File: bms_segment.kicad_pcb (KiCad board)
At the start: 4 copper layers, 100 x 67 mm, 167 parts, among them J1 Conn_01x13, J2 Conn_01x04, J3 Conn_02x10_Odd_Even, J4 Conn_02x10_Odd_Even, J5 Conn_01x05, J6 Conn_01x04, Q1 IRLML0060, Q10 IRLML0060, Q11 IRLML0060, Q12 IRLML0060, Q2 IRLML0060, Q3 IRLML0060, Q4 IRLML0060, Q5 IRLML0060, Q6 IRLML0060, Q7 IRLML0060, Q8 IRLML0060, Q9 IRLML0060, SW1 SW_Push, U1 LMR516xx, U2 STM32F103C8Tx, U3 ADuM1252, U4 MAX14920, U5 MAX11163, U6 REF61xx, U7 TCA9535PWR, Y1 8M

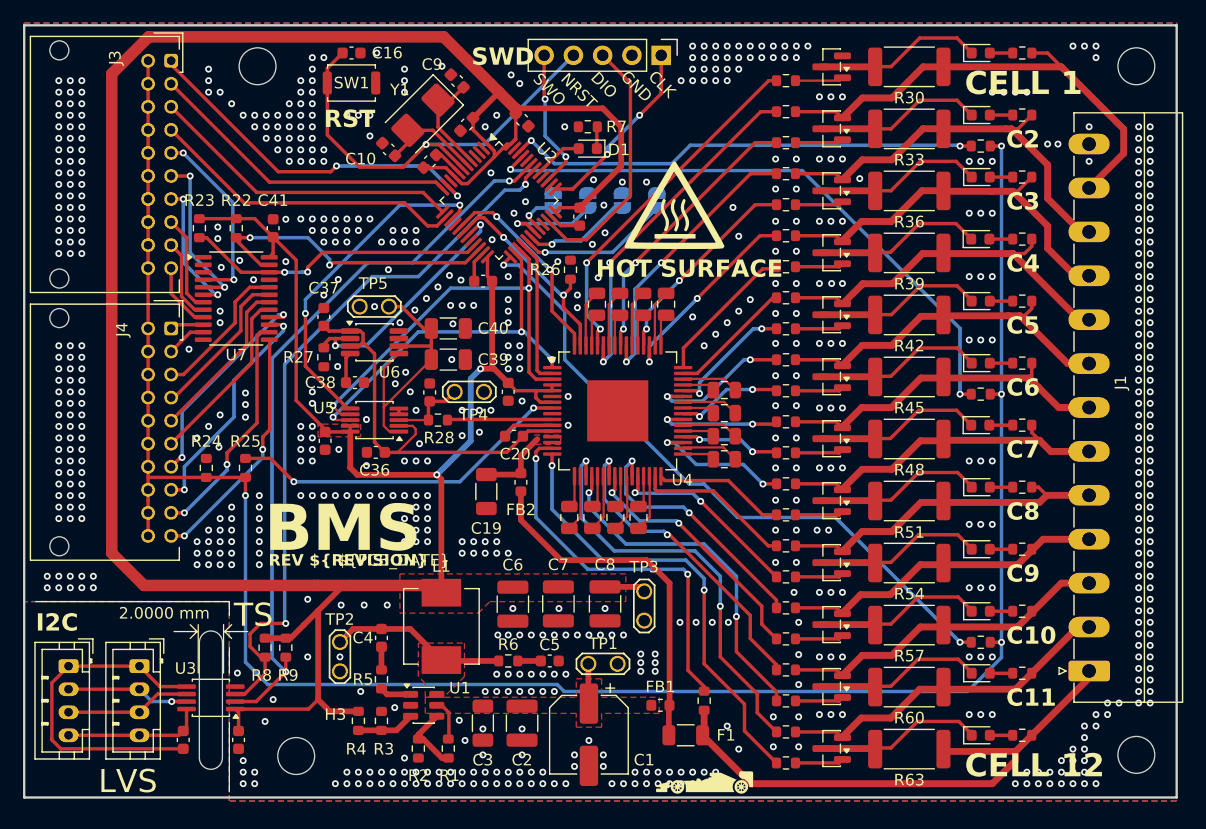
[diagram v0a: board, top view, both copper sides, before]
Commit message: *: Create a 3V3 plane and switch to new reset button
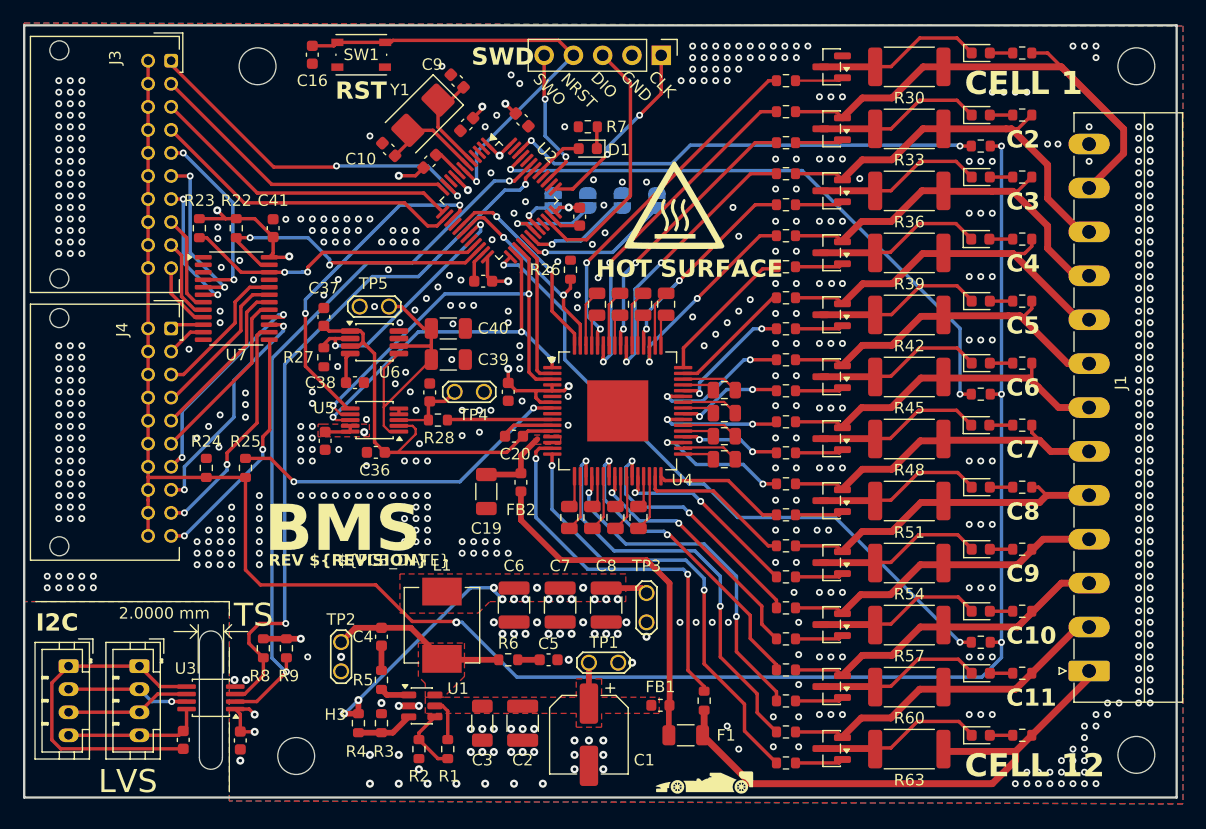
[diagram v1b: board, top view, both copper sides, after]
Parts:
- SW1: footprint Button_Switch_SMD:SW_Push_SPST_NO_Alps_SKRK -> Button_Switch_SMD:SW_Push_1P1T_NO_Vertical_Wuerth_434133025816
- moved C16 3.40 mm to (70.0, 56.8), turned to -90 degrees
- moved SW1 2.59 mm to (74.2, 56.8)
- moved TP3 0.25 mm to (99.0, 106.0)
- moved R3 0.20 mm to (76.0, 114.8)
- moved R4 0.20 mm to (74.0, 114.8)
- moved C7 0.18 mm to (91.5, 104.5)
- moved U1 0.17 mm to (79.5, 113.2)
- moved R8 0.16 mm to (65.8, 108.2)
- moved C17 0.16 mm to (63.8, 116.2)
- moved C8 0.14 mm to (95.5, 104.5)
- moved C5 0.14 mm to (90.5, 109.2)
- moved C6 0.12 mm to (87.5, 104.5)
- moved L1 0.11 mm to (81.2, 106.2)
- moved TP1 0.11 mm to (94.0, 109.5)
- moved TP2 0.10 mm to (72.5, 110.2)
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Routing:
- net +3V3: track 269.1 -> 73.7 mm, vias 2 -> 29
- net T2: track 181.0 -> 175.3 mm
- net /NRST: track 38.3 -> 39.0 mm
- net GND: vias 730 -> 607
- added copper zone on In2.Cu, net +3V3

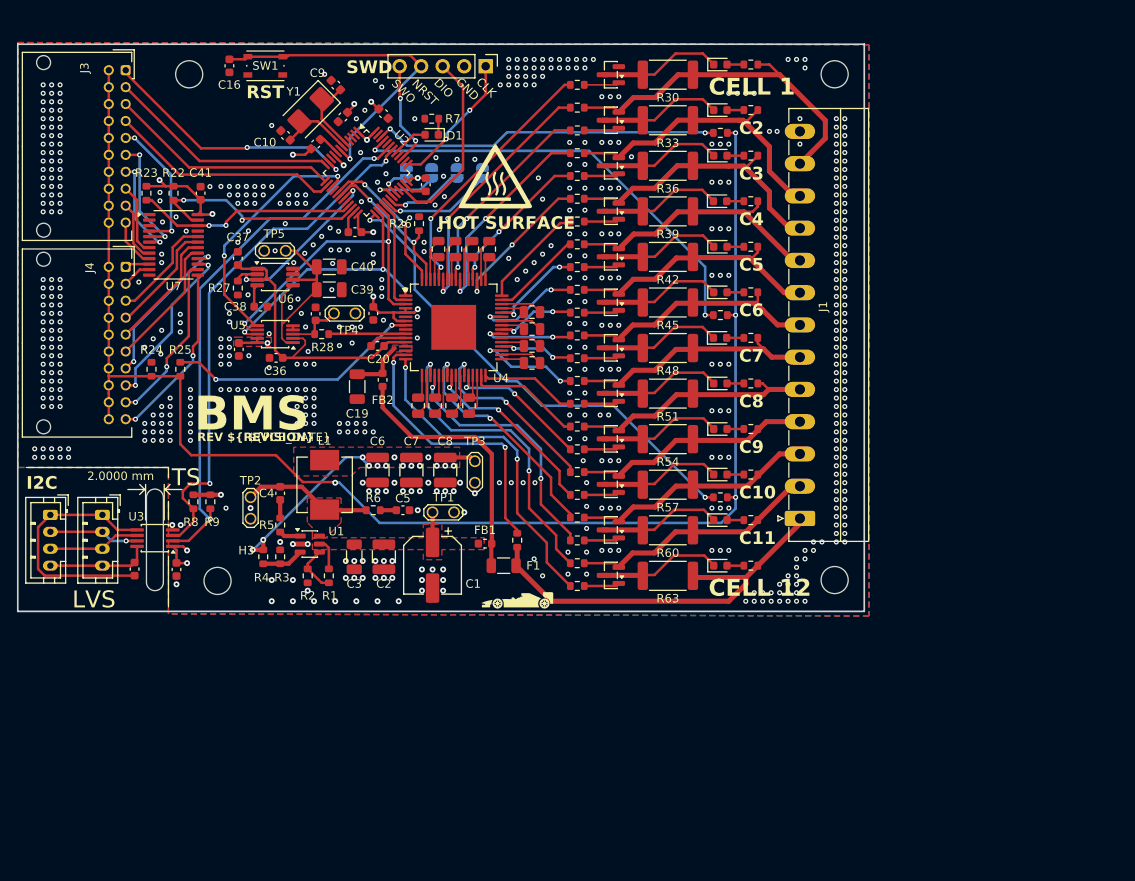
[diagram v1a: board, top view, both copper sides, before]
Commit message: pcb: Create blank PCB
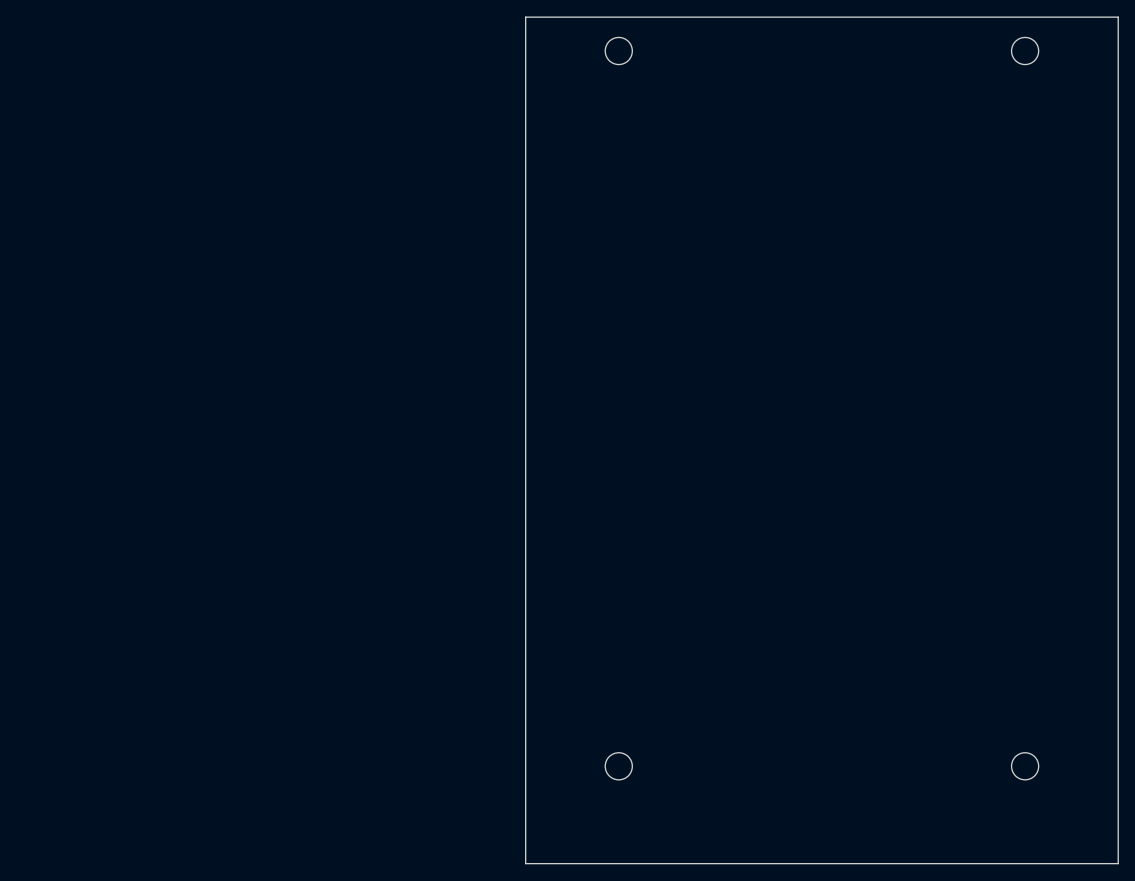
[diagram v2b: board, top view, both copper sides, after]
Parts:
- removed C1: 22u, Capacitor_SMD:CP_Elec_6.3x7.7
- removed C10, C9: 30p, Capacitor_SMD:C_0603_1608Metric
- removed C11, C12, C13, C14, C15, C20, C21, C38, C41: 1u, Capacitor_SMD:C_0603_1608Metric
- removed C16, C17, C18, C35, C36, C37, C4: 100n, Capacitor_SMD:C_0603_1608Metric
- removed C19, C3: 100n, Capacitor_SMD:C_1206_3216Metric
- removed C2: 2u2, Capacitor_SMD:C_1210_3225Metric
- removed C22, C23, C24, C25, C26, C27, C28, C29, C30, C31, C32, C33: 1u, Capacitor_SMD:C_0805_2012Metric
- removed C34: 100p, Capacitor_SMD:C_0603_1608Metric
- removed C39, C40: 10u, Capacitor_SMD:C_1206_3216Metric
- removed C5: ?, Capacitor_SMD:C_0603_1608Metric
- removed C6, C7, C8: 22u, Capacitor_SMD:C_1210_3225Metric
- removed D1, D10, D11, D12, D13, D2, D3, D4, D5, D6, D7, D8, D9: LED_Small, LED_SMD:LED_0603_1608Metric
- removed F1: Polyfuse, Resistor_SMD:R_1206_3216Metric
- removed FB1: 600, Inductor_SMD:L_0603_1608Metric
- removed FB2: 220, Inductor_SMD:L_0603_1608Metric
- removed G***, G****: LOGO, LOGO
- removed J1: Conn_01x13, Connector_Phoenix_MC:PhoenixContact_MC_1,5_13-G-3.81_1x13_P3.81mm_Horizontal
- removed J2, J6: Conn_01x04, Connector_JST:JST_PH_B4B-PH-K_1x04_P2.00mm_Vertical
- removed J3, J4: Conn_02x10_Odd_Even, Connector_JST:JST_PUD_S20B-PUDSS-1_2x10_P2.00mm_Horizontal
- removed J5: Conn_01x05, Connector_PinHeader_2.54mm:PinHeader_1x05_P2.54mm_Vertical
- removed JP1, JP2, JP3, JP4: SolderJumper_2_Open, Jumper:SolderJumper-2_P1.3mm_Open_RoundedPad1.0x1.5mm
- removed L1: 22u, Inductor_SMD:L_Vishay_IHLP-2525
- removed Q1, Q10, Q11, Q12, Q2, Q3, Q4, Q5, Q6, Q7, Q8, Q9: IRLML0060, Package_TO_SOT_SMD:SOT-23
- removed R1: 10M, Resistor_SMD:R_0603_1608Metric
- removed R10, R11, R12, R13, R14, R15, R16, R17, R18, R19, R20, R21, R29, R32, R35, R38, R41, R44, R47, R50, R53, R56, R59, R62: 3k, Resistor_SMD:R_0603_1608Metric
- removed R2: 390k, Resistor_SMD:R_0603_1608Metric
- removed R22, R23, R26, R27, R8, R9: 100k, Resistor_SMD:R_0603_1608Metric
- removed R24, TH1, TH2, TH3: 10k, Resistor_SMD:R_0603_1608Metric
- removed R25: 1k, Resistor_SMD:R_0603_1608Metric
- removed R28: 220, Resistor_SMD:R_0603_1608Metric
- removed R3: 24k, Resistor_SMD:R_0603_1608Metric
- removed R30, R33, R36, R39, R42, R45, R48, R51, R54, R57, R60, R63: 20, Resistor_SMD:R_2512_6332Metric
- removed R31, R34, R37, R40, R43, R46, R49, R52, R55, R58, R61, R64, R7: 330, Resistor_SMD:R_0603_1608Metric
- removed R4: 75k, Resistor_SMD:R_0603_1608Metric
- removed R5: 6R8, Resistor_SMD:R_0603_1608Metric
- removed R6: ?, Resistor_SMD:R_0603_1608Metric
- removed SW1: SW_Push, Button_Switch_SMD:SW_Push_1P1T_NO_Vertical_Wuerth_434133025816
- removed TP1, TP2, TP3, TP4, TP5: TestPoint_2Pole, yfs:TestPoint_2Pads_Pitch2.54mm_Drill1.0mm
- removed U1: LMR516xx, Package_TO_SOT_SMD:SOT-23-6
- removed U2: STM32F103C8Tx, Package_QFP:LQFP-48_7x7mm_P0.5mm
- removed U3: ADuM1252, Package_SO:MSOP-8_3x3mm_P0.65mm
- removed U4: MAX14920, Package_QFP:TQFP-64-1EP_10x10mm_P0.5mm_EP5.305x5.305mm
- removed U5: MAX11163, Package_SO:MSOP-10_3x3mm_P0.5mm
- removed U6: REF61xx, Package_SO:VSSOP-8_3x3mm_P0.65mm
- removed U7: TCA9535PWR, Package_SO:TSSOP-24_4.4x7.8mm_P0.65mm
- removed Y1: 8M, Crystal:Crystal_SMD_5032-2Pin_5.0x3.2mm
- moved H4 128.2 mm to (164.0, 139.5)
- moved H1 67.5 mm to (116.0, 55.0)
- moved H3 52.2 mm to (116.0, 139.5)
- moved H2 22.7 mm to (164.0, 55.0)
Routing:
- net T2: track 175.3 -> 0.00 mm, vias 4 -> 0
- net +3V3: track 73.7 -> 0.00 mm, vias 29 -> 0
- net /SDA: track 63.9 -> 0.00 mm, vias 2 -> 0
- net /SCL: track 62.4 -> 0.00 mm, vias 2 -> 0
- net /Thermistors/TH2: track 57.6 -> 0.00 mm, vias 2 -> 0
- net /Thermistors/TH1: track 53.0 -> 0.00 mm, vias 2 -> 0
- net TAP12: track 48.7 -> 0.00 mm
- net TAP1: track 42.2 -> 0.00 mm
- net /Thermistors/TH0: track 41.2 -> 0.00 mm, vias 2 -> 0
- net BA12: track 39.1 -> 0.00 mm, vias 2 -> 0
- net /NRST: track 39.0 -> 0.00 mm, vias 1 -> 0
- net Net-(U4-CV11): track 36.3 -> 0.00 mm, vias 2 -> 0
- net MISO: track 36.2 -> 0.00 mm, vias 2 -> 0
- net TAP3: track 35.9 -> 0.00 mm
- net TAP2: track 35.7 -> 0.00 mm
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- removed copper zone on F.Cu, net +3V3
- removed copper zone on In2.Cu, net +3V3
- removed copper zone on F.Cu, net /AFE_VIN
- removed copper zone on F.Cu, net /BUCK_SW
- removed copper zone on F.Cu, net /BUCK_VIN
- removed copper zone on B.Cu, net GND
- removed copper zone on F.Cu, net GND
- removed copper zone on In1.Cu, net GND
- removed copper zone on In2.Cu, net GND
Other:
- board size 100 x 67 mm -> 70 x 100 mm
- board text removed: "${PCB_DATE}"
- board text removed: "2.0000 mm"
- board text removed: "A0"
- board text removed: "A1"
- board text removed: "A2"
- board text removed: "A3"
- board text removed: "BMS"
- board text removed: "BY LOGAN C + OWEN S"
- board text removed: "C10"
- board text removed: "C11"
- board text removed: "C2"
- board text removed: "C3"
- board text removed: "C4"
- board text removed: "C5"
- board text removed: "C6"
- board text removed: "C7"
- board text removed: "C8"
- board text removed: "C9"
- board text removed: "CELL 1"
- board text removed: "CELL 12"
- board text removed: "CLK"
- board text removed: "DIO"
- board text removed: "DISTRIBUTED BMS"
- board text removed: "GND"
- board text removed: "HOT SURFACE"
- board text removed: "I2C"
- board text removed: "LVS"
- board text removed: "NRST"
- board text removed: "REV ${REVISION}"
- board text removed: "RST"
- board text removed: "SWD"
- board text removed: "SWO"
- board text removed: "TS"
- board text removed: "{ "ViaStitching": "0.2", "stitch_zone_0": { "HSpacing": "1", "VSpacing": "1", "HOffset": "0", "VOffset": "", "Clearance": "1", "Randomize": true } }"
- board text removed: "{ "ViaStitching": "0.2", "stitch_zone_0": { "HSpacing": "1", "VSpacing": "1", "HOffset": "0", "VOffset": "0", "Clearance": "0.75", "Randomize": false } }"
- board text removed: "{ "ViaStitching": "0.2", "stitch_zone_0": { "HSpacing": "1", "VSpacing": "1", "HOffset": "0", "VOffset": "0", "Clearance": "1", "Randomize": false } }"
- board text removed: "{ "ViaStitching": "0.2", "stitch_zone_0": { "HSpacing": "2", "VSpacing": "2", "HOffset": "1", "VOffset": "1", "Clearance": "0", "Randomize": false } }"

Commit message: pcb: Add progress so far
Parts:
- added C1: 22u, Capacitor_SMD:CP_Elec_6.3x7.7, F.Cu at (135.2, 52.5)
- added C10: 1u, Capacitor_SMD:C_0603_1608Metric, F.Cu at (41.3, 101.0)
- added C11: 100n, Capacitor_SMD:C_1206_3216Metric, F.Cu at (86.5, 111.0)
- added C12: 1u, Capacitor_SMD:C_0805_2012Metric, F.Cu at (61.5, 98.8)
- added C13: 1u, Capacitor_SMD:C_0805_2012Metric, F.Cu at (61.5, 101.8)
- added C14: 1u, Capacitor_SMD:C_0805_2012Metric, F.Cu at (61.5, 104.8)
- added C15: 1u, Capacitor_SMD:C_0805_2012Metric, F.Cu at (61.5, 107.8)
- added C16: 1u, Capacitor_SMD:C_0805_2012Metric, F.Cu at (66.0, 98.8)
- added C17: 1u, Capacitor_SMD:C_0805_2012Metric, F.Cu at (66.0, 101.8)
- added C18: 1u, Capacitor_SMD:C_0805_2012Metric, F.Cu at (66.0, 104.8)
- added C19: 1u, Capacitor_SMD:C_0805_2012Metric, F.Cu at (66.0, 107.8)
- added C2: 2u2, Capacitor_SMD:C_1210_3225Metric, F.Cu at (141.0, 53.5)
- added C20: 1u, Capacitor_SMD:C_0805_2012Metric, F.Cu at (70.4, 98.8)
- added C21: 1u, Capacitor_SMD:C_0805_2012Metric, F.Cu at (70.4, 101.8)
- added C22: 1u, Capacitor_SMD:C_0805_2012Metric, F.Cu at (70.4, 104.8)
- added C23: 1u, Capacitor_SMD:C_0805_2012Metric, F.Cu at (70.4, 107.8)
- added C24: 1u, Capacitor_SMD:C_0805_2012Metric, F.Cu at (74.9, 98.8)
- added C25: 1u, Capacitor_SMD:C_0805_2012Metric, F.Cu at (74.9, 101.8)
- added C26: 1u, Capacitor_SMD:C_0805_2012Metric, F.Cu at (74.9, 104.8)
- added C27: 1u, Capacitor_SMD:C_0805_2012Metric, F.Cu at (74.9, 107.8)
- added C28: 100p, Capacitor_SMD:C_0603_1608Metric, F.Cu at (45.3, 103.5)
- added C29: 100n, Capacitor_SMD:C_0603_1608Metric, F.Cu at (45.3, 108.5)
- added C3: 100n, Capacitor_SMD:C_1206_3216Metric, F.Cu at (144.5, 53.5)
- added C30: 100n, Capacitor_SMD:C_0603_1608Metric, F.Cu at (45.3, 111.0)
- added C31: 100n, Capacitor_SMD:C_0603_1608Metric, F.Cu at (45.3, 113.6)
- added C32: 1u, Capacitor_SMD:C_0603_1608Metric, F.Cu at (45.3, 106.0)
- added C33: 10u, Capacitor_SMD:C_1206_3216Metric, F.Cu at (86.5, 114.3)
- added C34: 10u, Capacitor_SMD:C_1206_3216Metric, F.Cu at (86.5, 117.7)
- added C35: 1u, Capacitor_SMD:C_0603_1608Metric, F.Cu at (41.3, 106.0)
- added C36: 1u, Capacitor_SMD:C_0603_1608Metric, F.Cu at (41.3, 111.0)
- added C37: 1u, Capacitor_SMD:C_0603_1608Metric, F.Cu at (41.3, 113.6)
- added C38: 1u, Capacitor_SMD:C_0603_1608Metric, F.Cu at (41.3, 116.1)
- added C39: 1u, Capacitor_SMD:C_0603_1608Metric, F.Cu at (45.3, 98.5)
- added C4: 100n, Capacitor_SMD:C_0603_1608Metric, F.Cu at (153.2, 61.0)
- added C40: 100n, Capacitor_SMD:C_0603_1608Metric, F.Cu at (45.3, 101.0)
- added C41: 100n, Capacitor_SMD:C_0603_1608Metric, F.Cu at (41.3, 103.5)
- added C42: 100n, Capacitor_SMD:C_0603_1608Metric, F.Cu at (41.3, 108.5)
- added C43: ?, Capacitor_SMD:C_0603_1608Metric, F.Cu at (76.4, 127.3)
- added C44: ?, Capacitor_SMD:C_0603_1608Metric, F.Cu at (76.4, 129.8)
- added C45: ?, Capacitor_SMD:C_0603_1608Metric, F.Cu at (76.4, 132.4)
- added C46: ?, Capacitor_SMD:C_0603_1608Metric, F.Cu at (76.4, 134.9)
- added C47: 1u, Capacitor_SMD:C_0603_1608Metric, F.Cu at (93.2, 98.0)
- added C48: 1u, Capacitor_SMD:C_0603_1608Metric, F.Cu at (93.2, 100.5)
- added C49: 1u, Capacitor_SMD:C_0603_1608Metric, F.Cu at (93.2, 103.0)
- added C5: ?, Capacitor_SMD:C_0603_1608Metric, F.Cu at (138.8, 59.0)
- added C6: 22u, Capacitor_SMD:C_1210_3225Metric, F.Cu at (141.8, 63.8)
- added C7: 22u, Capacitor_SMD:C_1210_3225Metric, F.Cu at (137.8, 63.8)
- added C8: 22u, Capacitor_SMD:C_1210_3225Metric, F.Cu at (133.8, 63.8)
- added C9: 1u, Capacitor_SMD:C_0603_1608Metric, F.Cu at (41.3, 98.5)
- added D1: LED_Small, LED_SMD:LED_0603_1608Metric, F.Cu at (122.0, 132.0)
- added D10: LED_Small, LED_SMD:LED_0603_1608Metric, F.Cu at (122.0, 91.5)
- added D11: LED_Small, LED_SMD:LED_0603_1608Metric, F.Cu at (122.0, 87.0)
- added D12: LED_Small, LED_SMD:LED_0603_1608Metric, F.Cu at (122.0, 82.5)
- added D13: LED_Small, LED_SMD:LED_0603_1608Metric, F.Cu at (122.0, 78.0)
- added D14: LED_Small, LED_SMD:LED_0603_1608Metric, F.Cu at (123.0, 73.5)
- added D15: LED_Small, LED_SMD:LED_0603_1608Metric, F.Cu at (123.0, 69.0)
- added D16: LED_Small, LED_SMD:LED_0603_1608Metric, F.Cu at (123.0, 64.5)
- added D17: LED_Small, LED_SMD:LED_0603_1608Metric, F.Cu at (54.9, 121.9)
- added D18: BYG20J, Diode_SMD:D_SMA, F.Cu at (164.0, 82.5)
- added D19: BYG20J, Diode_SMD:D_SMA, F.Cu at (82.5, 128.4)
- added D2: LED_Small, LED_SMD:LED_0603_1608Metric, F.Cu at (122.0, 127.5)
- added D20: BYG20J, Diode_SMD:D_SMA, F.Cu at (82.5, 132.9)
- added D3: LED_Small, LED_SMD:LED_0603_1608Metric, F.Cu at (122.0, 123.0)
- added D4: LED_Small, LED_SMD:LED_0603_1608Metric, F.Cu at (122.0, 118.5)
- added D5: LED_Small, LED_SMD:LED_0603_1608Metric, F.Cu at (122.0, 114.0)
- added D6: LED_Small, LED_SMD:LED_0603_1608Metric, F.Cu at (122.0, 109.5)
- added D7: LED_Small, LED_SMD:LED_0603_1608Metric, F.Cu at (122.0, 105.0)
- added D8: LED_Small, LED_SMD:LED_0603_1608Metric, F.Cu at (122.0, 100.5)
- added D9: LED_Small, LED_SMD:LED_0603_1608Metric, F.Cu at (122.0, 96.0)
- added F1: Polyfuse, Resistor_SMD:R_1206_3216Metric, F.Cu at (55.6, 119.0)
- added F2: Polyfuse, Resistor_SMD:R_1206_3216Metric, F.Cu at (164.0, 71.5)
- added FB1: 600, Inductor_SMD:L_0603_1608Metric, F.Cu at (129.1, 55.1)
- added FB2: 220, Inductor_SMD:L_0603_1608Metric, F.Cu at (45.3, 116.1)
- added J1: Conn_02x09_Counter_Clockwise, yfs:MolexMilliGrid2x9, F.Cu at (81.7, 62.6)
- added J2: Conn_02x09_Counter_Clockwise, yfs:MolexMilliGrid2x9, F.Cu at (133.4, 82.8)
- added J3: Conn_02x10_Odd_Even, Connector_JST:JST_PUD_S20B-PUDSS-1_2x10_P2.00mm_Horizontal, F.Cu at (162.2, 132.5)
- added J4: Conn_02x10_Odd_Even, Connector_JST:JST_PUD_S20B-PUDSS-1_2x10_P2.00mm_Horizontal, F.Cu at (162.2, 108.0)
- added J5: Conn_01x04, Connector_JST:JST_PH_B4B-PH-K_1x04_P2.00mm_Vertical, F.Cu at (109.0, 141.0)
- added J6: Conn_01x04, Connector_JST:JST_PH_B4B-PH-K_1x04_P2.00mm_Vertical, F.Cu at (62.3, 119.1)
- added J7: Conn_01x06, yfs:IDC-Connector-2x3, F.Cu at (64.8, 113.3)
- added JP1: SolderJumper_2_Open, Jumper:SolderJumper-2_P1.3mm_Open_RoundedPad1.0x1.5mm, F.Cu at (81.5, 111.1)
- added JP2: SolderJumper_2_Open, Jumper:SolderJumper-2_P1.3mm_Open_RoundedPad1.0x1.5mm, F.Cu at (81.5, 114.6)
- added JP3: SolderJumper_2_Open, Jumper:SolderJumper-2_P1.3mm_Open_RoundedPad1.0x1.5mm, F.Cu at (81.5, 118.2)
- added JP4: SolderJumper_2_Open, Jumper:SolderJumper-2_P1.3mm_Open_RoundedPad1.0x1.5mm, F.Cu at (81.5, 121.7)
- added L1: 22u, Inductor_SMD:L_Vishay_IHLP-2525, F.Cu at (148.0, 62.0)
- added Q1: IRLML0060, Package_TO_SOT_SMD:SOT-23, F.Cu at (109.5, 131.0)
- added Q10: IRLML0060, Package_TO_SOT_SMD:SOT-23, F.Cu at (109.5, 90.5)
- added Q11: IRLML0060, Package_TO_SOT_SMD:SOT-23, F.Cu at (109.5, 86.0)
- added Q12: IRLML0060, Package_TO_SOT_SMD:SOT-23, F.Cu at (109.5, 81.5)
- added Q13: IRLML0060, Package_TO_SOT_SMD:SOT-23, F.Cu at (109.5, 77.0)
- added Q14: IRLML0060, Package_TO_SOT_SMD:SOT-23, F.Cu at (109.5, 72.5)
- added Q15: IRLML0060, Package_TO_SOT_SMD:SOT-23, F.Cu at (109.5, 68.0)
- added Q16: IRLML0060, Package_TO_SOT_SMD:SOT-23, F.Cu at (109.5, 63.5)
- added Q17: BSS84, Package_TO_SOT_SMD:SOT-23, F.Cu at (164.0, 76.5)
- added Q2: IRLML0060, Package_TO_SOT_SMD:SOT-23, F.Cu at (109.5, 126.5)
- added Q3: IRLML0060, Package_TO_SOT_SMD:SOT-23, F.Cu at (109.5, 122.0)
- added Q4: IRLML0060, Package_TO_SOT_SMD:SOT-23, F.Cu at (109.5, 117.5)
- added Q5: IRLML0060, Package_TO_SOT_SMD:SOT-23, F.Cu at (109.5, 113.0)
- added Q6: IRLML0060, Package_TO_SOT_SMD:SOT-23, F.Cu at (109.5, 108.5)
- added Q7: IRLML0060, Package_TO_SOT_SMD:SOT-23, F.Cu at (109.5, 104.0)
- added Q8: IRLML0060, Package_TO_SOT_SMD:SOT-23, F.Cu at (109.5, 99.5)
- added Q9: IRLML0060, Package_TO_SOT_SMD:SOT-23, F.Cu at (109.5, 95.0)
- added R1: 10M, Resistor_SMD:R_0603_1608Metric, F.Cu at (147.5, 51.3)
- added R10: 3k, Resistor_SMD:R_0603_1608Metric, F.Cu at (49.3, 101.0)
- added R11: 3k, Resistor_SMD:R_0603_1608Metric, F.Cu at (49.3, 103.5)
- added R12: 3k, Resistor_SMD:R_0603_1608Metric, F.Cu at (49.3, 106.0)
- added R13: 3k, Resistor_SMD:R_0603_1608Metric, F.Cu at (49.3, 108.5)
- added R14: 3k, Resistor_SMD:R_0603_1608Metric, F.Cu at (49.3, 111.0)
- added R15: 3k, Resistor_SMD:R_0603_1608Metric, F.Cu at (49.3, 113.6)
- added R16: 3k, Resistor_SMD:R_0603_1608Metric, F.Cu at (49.3, 116.1)
- added R17: 3k, Resistor_SMD:R_0603_1608Metric, F.Cu at (53.3, 98.5)
- added R18: 3k, Resistor_SMD:R_0603_1608Metric, F.Cu at (53.3, 101.0)
- added R19: 3k, Resistor_SMD:R_0603_1608Metric, F.Cu at (53.3, 106.0)
- added R2: 390k, Resistor_SMD:R_0603_1608Metric, F.Cu at (150.0, 51.3)
- added R20: 3k, Resistor_SMD:R_0603_1608Metric, F.Cu at (53.3, 108.5)
- added R21: 3k, Resistor_SMD:R_0603_1608Metric, F.Cu at (53.3, 113.6)
- added R22: 3k, Resistor_SMD:R_0603_1608Metric, F.Cu at (53.3, 116.1)
- added R23: 10k, Resistor_SMD:R_0603_1608Metric, F.Cu at (57.3, 98.5)
- added R24: 10k, Resistor_SMD:R_0603_1608Metric, F.Cu at (57.3, 103.5)
- added R25: 220, Resistor_SMD:R_0603_1608Metric, F.Cu at (57.3, 106.0)
- added R26: 10k, Resistor_SMD:R_0603_1608Metric, F.Cu at (57.3, 108.5)
- added R27: 3k, Resistor_SMD:R_0603_1608Metric, F.Cu at (106.5, 131.0)
- added R28: 20, Resistor_SMD:R_2512_6332Metric, F.Cu at (116.0, 131.0)
- added R29: 330, Resistor_SMD:R_0603_1608Metric, F.Cu at (125.5, 132.0)
- added R3: 24k, Resistor_SMD:R_0603_1608Metric, F.Cu at (153.2, 53.5)
- added R30: 3k, Resistor_SMD:R_0603_1608Metric, F.Cu at (106.5, 126.5)
- added R31: 20, Resistor_SMD:R_2512_6332Metric, F.Cu at (116.0, 126.5)
- added R32: 330, Resistor_SMD:R_0603_1608Metric, F.Cu at (125.5, 127.5)
- added R33: 3k, Resistor_SMD:R_0603_1608Metric, F.Cu at (106.5, 122.0)
- added R34: 20, Resistor_SMD:R_2512_6332Metric, F.Cu at (116.0, 122.0)
- added R35: 330, Resistor_SMD:R_0603_1608Metric, F.Cu at (125.5, 123.0)
- added R36: 3k, Resistor_SMD:R_0603_1608Metric, F.Cu at (106.5, 117.5)
- added R37: 20, Resistor_SMD:R_2512_6332Metric, F.Cu at (116.0, 117.5)
- added R38: 330, Resistor_SMD:R_0603_1608Metric, F.Cu at (125.5, 118.5)
- added R39: 3k, Resistor_SMD:R_0603_1608Metric, F.Cu at (106.5, 113.0)
- added R4: 75k, Resistor_SMD:R_0603_1608Metric, F.Cu at (155.2, 53.5)
- added R40: 20, Resistor_SMD:R_2512_6332Metric, F.Cu at (116.0, 113.0)
- added R41: 330, Resistor_SMD:R_0603_1608Metric, F.Cu at (125.5, 114.0)
- added R42: 3k, Resistor_SMD:R_0603_1608Metric, F.Cu at (106.5, 108.5)
- added R43: 20, Resistor_SMD:R_2512_6332Metric, F.Cu at (116.0, 108.5)
- added R44: 330, Resistor_SMD:R_0603_1608Metric, F.Cu at (125.5, 109.5)
- added R45: 3k, Resistor_SMD:R_0603_1608Metric, F.Cu at (106.5, 104.0)
- added R46: 20, Resistor_SMD:R_2512_6332Metric, F.Cu at (116.0, 104.0)
- added R47: 330, Resistor_SMD:R_0603_1608Metric, F.Cu at (125.5, 105.0)
- added R48: 3k, Resistor_SMD:R_0603_1608Metric, F.Cu at (106.5, 99.5)
- added R49: 20, Resistor_SMD:R_2512_6332Metric, F.Cu at (116.0, 99.5)
- added R5: 6R8, Resistor_SMD:R_0603_1608Metric, F.Cu at (153.2, 57.3)
- added R50: 330, Resistor_SMD:R_0603_1608Metric, F.Cu at (125.5, 100.5)
- added R51: 3k, Resistor_SMD:R_0603_1608Metric, F.Cu at (106.5, 95.0)
- added R52: 20, Resistor_SMD:R_2512_6332Metric, F.Cu at (116.0, 95.0)
- added R53: 330, Resistor_SMD:R_0603_1608Metric, F.Cu at (125.5, 96.0)
- added R54: 3k, Resistor_SMD:R_0603_1608Metric, F.Cu at (106.5, 90.5)
- added R55: 20, Resistor_SMD:R_2512_6332Metric, F.Cu at (116.0, 90.5)
- added R56: 330, Resistor_SMD:R_0603_1608Metric, F.Cu at (125.5, 91.5)
- added R57: 3k, Resistor_SMD:R_0603_1608Metric, F.Cu at (106.5, 86.0)
- added R58: 20, Resistor_SMD:R_2512_6332Metric, F.Cu at (116.0, 86.0)
- added R59: 330, Resistor_SMD:R_0603_1608Metric, F.Cu at (125.5, 87.0)
- added R6: ?, Resistor_SMD:R_0603_1608Metric, F.Cu at (142.2, 59.0)
- added R60: 3k, Resistor_SMD:R_0603_1608Metric, F.Cu at (106.5, 81.5)
- added R61: 20, Resistor_SMD:R_2512_6332Metric, F.Cu at (116.0, 81.5)
- added R62: 330, Resistor_SMD:R_0603_1608Metric, F.Cu at (125.5, 82.5)
- added R63: 3k, Resistor_SMD:R_0603_1608Metric, F.Cu at (106.5, 77.0)
- added R64: 20, Resistor_SMD:R_2512_6332Metric, F.Cu at (116.0, 77.0)
- added R65: 330, Resistor_SMD:R_0603_1608Metric, F.Cu at (122.0, 76.0)
- added R66: 3k, Resistor_SMD:R_0603_1608Metric, F.Cu at (106.5, 72.5)
- added R67: 20, Resistor_SMD:R_2512_6332Metric, F.Cu at (116.0, 72.5)
- added R68: 330, Resistor_SMD:R_0603_1608Metric, F.Cu at (125.0, 73.5)
- added R69: 3k, Resistor_SMD:R_0603_1608Metric, F.Cu at (106.5, 68.0)
- added R7: 3k, Resistor_SMD:R_0603_1608Metric, F.Cu at (135.5, 96.5)
- added R70: 20, Resistor_SMD:R_2512_6332Metric, F.Cu at (116.0, 68.0)
- added R71: 330, Resistor_SMD:R_0603_1608Metric, F.Cu at (125.0, 69.0)
- added R72: 3k, Resistor_SMD:R_0603_1608Metric, F.Cu at (106.5, 63.5)
- added R73: 20, Resistor_SMD:R_2512_6332Metric, F.Cu at (116.0, 63.5)
- added R74: 330, Resistor_SMD:R_0603_1608Metric, F.Cu at (125.0, 64.5)
- added R75: 10k, Resistor_SMD:R_0603_1608Metric, F.Cu at (97.1, 135.7)
- added R76: 10k, Resistor_SMD:R_0603_1608Metric, F.Cu at (97.1, 138.2)
- added R77: 330, Resistor_SMD:R_0603_1608Metric, F.Cu at (57.3, 101.0)
- added R78: 10k, Resistor_SMD:R_0603_1608Metric, F.Cu at (53.3, 103.5)
- added R79: 10k, Resistor_SMD:R_0603_1608Metric, F.Cu at (53.3, 111.0)
- added R8: 3k, Resistor_SMD:R_0603_1608Metric, F.Cu at (137.5, 96.5)
- added R80: 10k, Resistor_SMD:R_0603_1608Metric, F.Cu at (76.4, 137.4)
- added R81: 10k, Resistor_SMD:R_0603_1608Metric, F.Cu at (76.4, 139.9)
- added R9: 3k, Resistor_SMD:R_0603_1608Metric, F.Cu at (49.3, 98.5)
- added RN1: R_Pack04, Resistor_SMD:R_Array_Convex_4x1206, F.Cu at (61.5, 130.0)
- added RN10: R_Pack04, Resistor_SMD:R_Array_Convex_4x1206, F.Cu at (61.5, 138.8)
- added RN11: R_Pack04, Resistor_SMD:R_Array_Convex_4x1206, F.Cu at (69.0, 130.0)
- added RN12: R_Pack04, Resistor_SMD:R_Array_Convex_4x1206, F.Cu at (69.0, 138.8)
- added RN2: R_Pack04, Resistor_SMD:R_Array_Convex_4x1206, F.Cu at (82.5, 100.3)
- added RN3: R_Pack04, Resistor_SMD:R_Array_Convex_4x1206, F.Cu at (157.0, 133.5)
- added RN4: R_Pack04, Resistor_SMD:R_Array_Convex_4x1206, F.Cu at (157.0, 128.5)
- added RN5: R_Pack04, Resistor_SMD:R_Array_Convex_4x1206, F.Cu at (157.0, 123.5)
- added RN6: R_Pack04, Resistor_SMD:R_Array_Convex_4x1206, F.Cu at (157.0, 118.5)
- added RN7: R_Pack04, Resistor_SMD:R_Array_Convex_4x1206, F.Cu at (157.0, 113.5)
- added RN8: R_Pack04, Resistor_SMD:R_Array_Convex_4x1206, F.Cu at (69.0, 147.5)
- added RN9: R_Pack04, Resistor_SMD:R_Array_Convex_4x1206, F.Cu at (61.5, 147.5)
- added SW1: SW_Push, Button_Switch_SMD:SW_Push_1P1T_NO_Vertical_Wuerth_434133025816, F.Cu at (87.1, 121.7)
- added TH1: 10k, Resistor_SMD:R_0603_1608Metric, F.Cu at (121.0, 65.0)
- added TH2: 10k, Resistor_SMD:R_0603_1608Metric, F.Cu at (51.2, 131.5)
- added TH3: 10k, Resistor_SMD:R_0603_1608Metric, F.Cu at (51.2, 134.0)
- added TH4: 10k, Resistor_SMD:R_0603_1608Metric, F.Cu at (51.2, 136.5)
- added TP1: TestPoint_2Pole, yfs:TestPoint_2Pads_Pitch2.54mm_Drill1.0mm, F.Cu at (135.2, 58.8)
- added TP2: TestPoint_2Pole, yfs:TestPoint_2Pads_Pitch2.54mm_Drill1.0mm, F.Cu at (156.8, 58.0)
- added TP3: TestPoint_2Pole, yfs:TestPoint_2Pads_Pitch2.54mm_Drill1.0mm, F.Cu at (130.2, 62.3)
- added TP4: TestPoint_2Pole, yfs:TestPoint_2Pads_Pitch2.54mm_Drill1.0mm, F.Cu at (41.1, 119.0)
- added TP5: TestPoint_2Pole, yfs:TestPoint_2Pads_Pitch2.54mm_Drill1.0mm, F.Cu at (41.1, 122.3)
- added U1: LMR516xx, Package_TO_SOT_SMD:SOT-23-6, F.Cu at (149.8, 55.0)
- added U2: MAX14921, Package_QFP:TQFP-80_12x12mm_P0.5mm, F.Cu at (149.0, 82.0)
- added U3: MAX11163, Package_SO:MSOP-10_3x3mm_P0.5mm, F.Cu at (75.7, 116.2)
- added U4: REF61xx, Package_SO:VSSOP-8_3x3mm_P0.65mm, F.Cu at (75.4, 121.0)
- added U5: STM32F103C8Tx, Package_QFP:LQFP-48_7x7mm_P0.5mm, F.Cu at (142.0, 142.5)
- added U6: ADuM1252, Package_SO:MSOP-8_3x3mm_P0.65mm, F.Cu at (75.7, 111.6)
- added U7: 74LV4051A, Package_SO:TSSOP-16_4.4x5mm_P0.65mm, F.Cu at (144.0, 131.0)
- added U8: 74LV4051A, Package_SO:TSSOP-16_4.4x5mm_P0.65mm, F.Cu at (143.5, 121.5)
- added U9: 74LV4051A, Package_SO:TSSOP-16_4.4x5mm_P0.65mm, F.Cu at (144.5, 112.5)
- added kibuzzard-69C6C1F9: G***, kibuzzard-69C6C1F9, F.Cu at (124.5, 62.3)
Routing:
- net +3V3: track 0.00 -> 25.6 mm, vias 0 -> 14
- net TAP15: track 0.00 -> 18.5 mm
- net TAP13: track 0.00 -> 16.1 mm
- net /BUCK_SW: track 0.00 -> 15.3 mm
- net TAP9: track 0.00 -> 11.9 mm
- net TAP8: track 0.00 -> 11.9 mm
- net TAP7: track 0.00 -> 11.9 mm
- net TAP6: track 0.00 -> 11.9 mm
- net TAP5: track 0.00 -> 11.9 mm
- net TAP4: track 0.00 -> 11.9 mm
- net TAP3: track 0.00 -> 11.9 mm
- net TAP2: track 0.00 -> 11.9 mm
- net TAP14: track 0.00 -> 11.9 mm
- net TAP12: track 0.00 -> 11.9 mm
- net TAP11: track 0.00 -> 11.9 mm
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- added copper zone on F.Cu, net +3V3
- added copper zone on F.Cu, net /BUCK_SW
- added copper zone on F.Cu, net /BUCK_VIN
